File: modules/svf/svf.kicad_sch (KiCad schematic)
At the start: 35 parts, among them U1 VTL5C, U2 VTL5C, U3 MCP6002-xSN, U4 MCP6002-xSN, U5 MCP6002-xSN

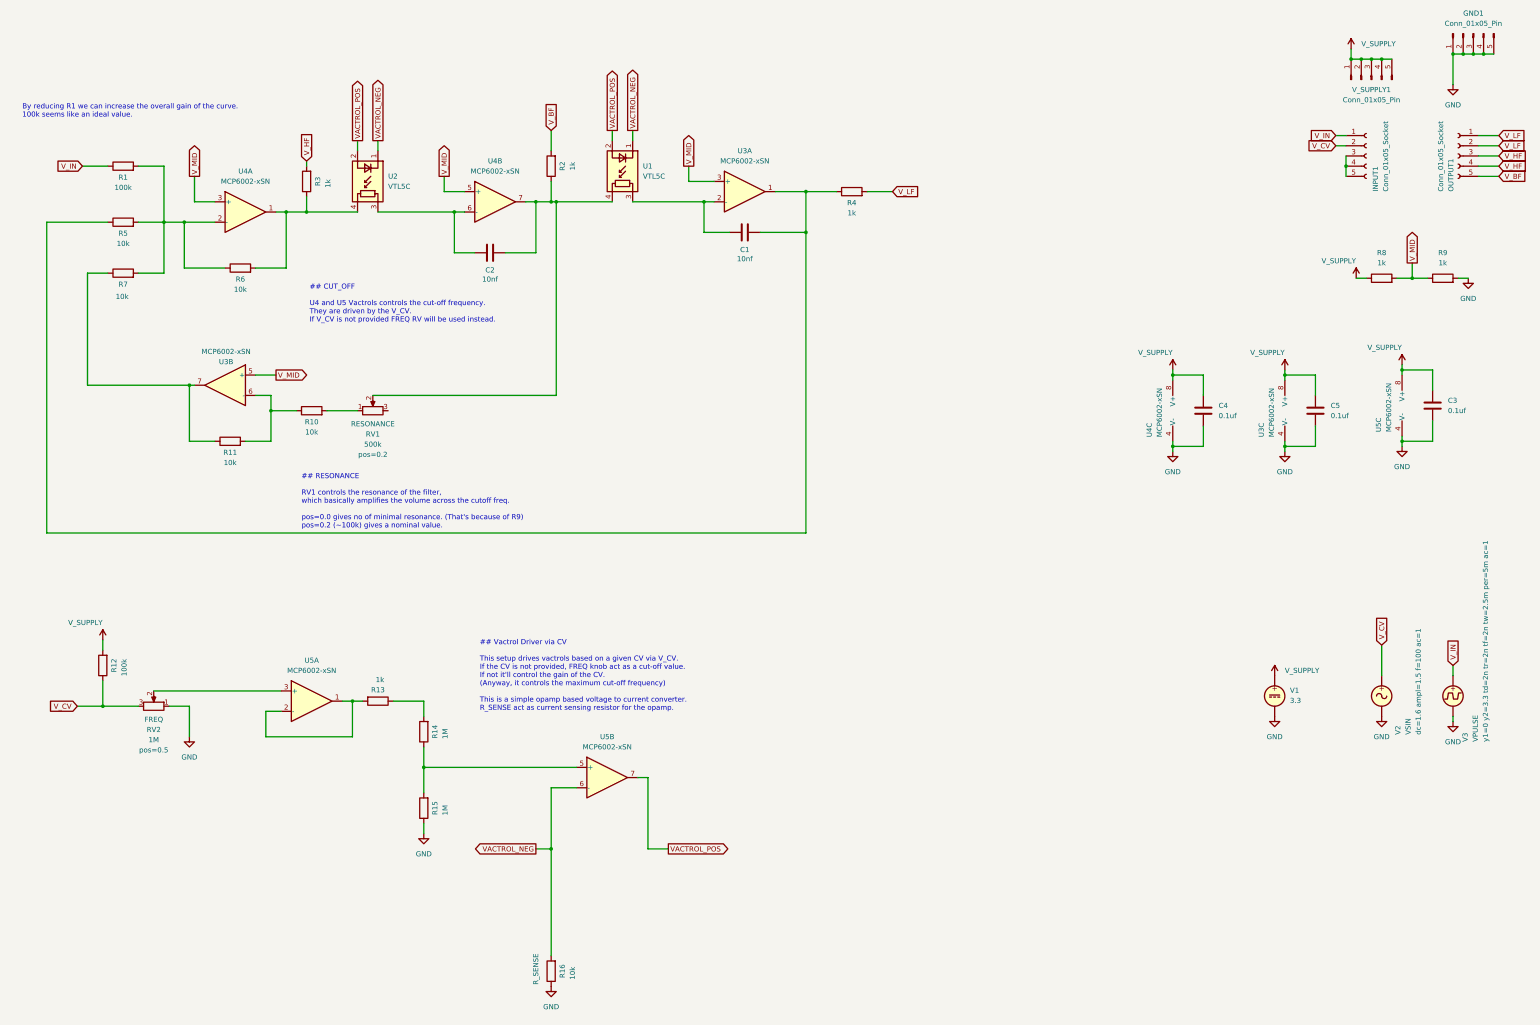
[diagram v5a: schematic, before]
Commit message: Finalized the PCB routing
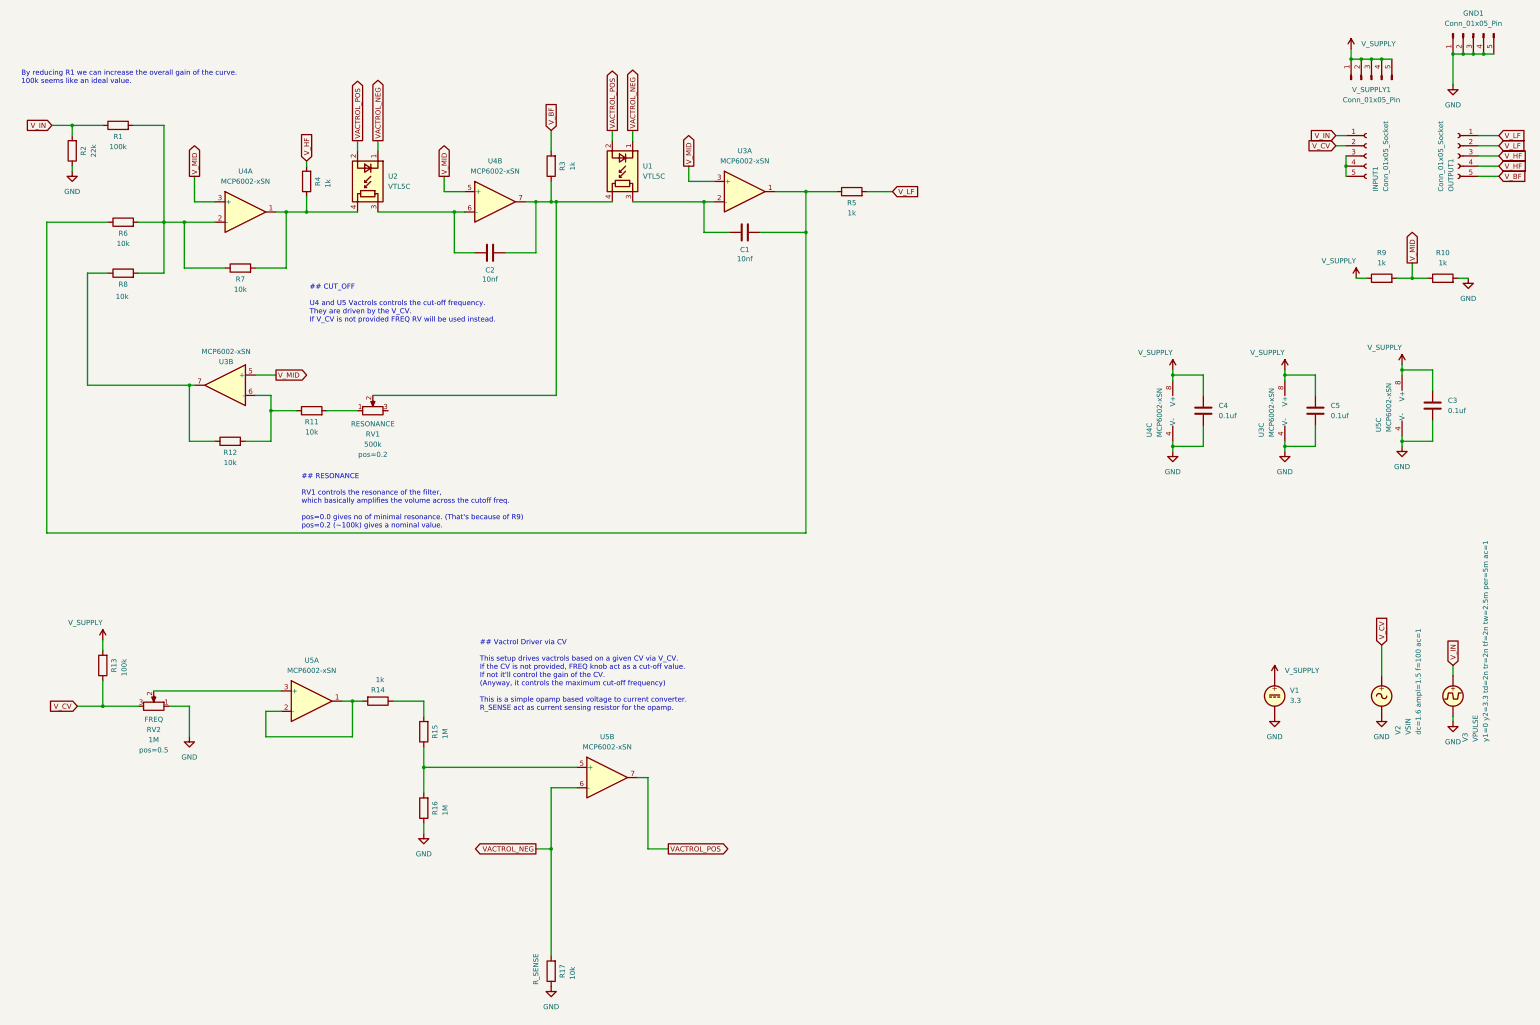
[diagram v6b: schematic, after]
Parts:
- added R2: 22k, Resistor_SMD:R_0402_1005Metric, symbol Device:R
- renumbered R9 to R10, R10 to R11, R11 to R12, R12 to R13, R13 to R14, R14 to R15, R15 to R16, R16 to R17, R2 to R3, R3 to R4, R4 to R5, R5 to R6, R6 to R7, R7 to R8, R8 to R9
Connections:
- net GND: now also R2.1
- net V_IN: now also R2.2
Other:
- moved on the sheet: R1

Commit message: svf: make it louder & add curve control Now the SVF is 8db louder in general. Now the resonance control active troughout the potentiometer Add the curve support for the freq so, we can target low or high based on the usage.
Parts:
- added RV3: 50k, BreadModular_Pots:Potentiometer_RV09, symbol Device:R_Potentiometer
- R1: value 100k -> 51k
- R11, R12: value 10k -> 51k
- R17: value 10k -> 5.1k
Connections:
- net VACTROL_NEG: now also RV3.1; no longer R17.2
- new net: R17.2, RV3.2
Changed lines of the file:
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@@
 	)
 	(junction
-		(at 153.67 226.06)
-		(diameter 0)
-		(color 0 0 0 0)
-	)
-	(junction
 		(at 381 27.94)
 		(diameter 0)
@@
 	)
 	(junction
+		(at 153.67 226.06)
+		(diameter 0)
+		(color 0 0 0 0)
+	)
+	(junction
 		(at 41.91 190.5)
 		(diameter 0)
@@
 	(wire
 		(pts
+			(xy 153.67 246.38) (xy 153.67 252.73)
+		)
+		(stroke
+			(width 0)
+			(type default)
+		)
+	)
+	(wire
+		(pts
 			(xy 27.94 147.32) (xy 217.17 147.32)
 		)
@@
 	(wire
 		(pts
+			(xy 161.29 242.57) (xy 153.67 242.57)
+		)
+		(stroke
+			(width 0)
+			(type default)
+		)
+	)
+	(wire
+		(pts
 			(xy 191.77 64.77) (xy 194.31 64.77)
 		)
@@
 	(wire
 		(pts
+			(xy 153.67 242.57) (xy 153.67 226.06)
+		)
+		(stroke
+			(width 0)
+			(type default)
+		)
+	)
+	(wire
+		(pts
 			(xy 316.23 107.95) (xy 308.61 107.95)
 		)
@@
 	(wire
 		(pts
-			(xy 153.67 226.06) (xy 153.67 252.73)
-		)
-		(stroke
-			(width 0)
-			(type default)
-		)
-	)
-	(wire
-		(pts
 			(xy 54.61 186.69) (xy 86.36 186.69)
 		)
@@
 	(wire
 		(pts
+			(xy 165.1 246.38) (xy 153.67 246.38)
+		)
+		(stroke
+			(width 0)
+			(type default)
+		)
+	)
+	(wire
+		(pts
 			(xy 127 62.23) (xy 127 58.42)
 		)
@@
 	(wire
 		(pts
+			(xy 109.22 113.03) (xy 154.94 113.03)
+		)
+		(stroke
+			(width 0)
+			(type default)
+		)
+	)
+	(wire
+		(pts
 			(xy 383.54 27.94) (xy 386.08 27.94)
 		)
@@
 	(wire
 		(pts
-			(xy 109.22 113.03) (xy 154.94 113.03)
-		)
-		(stroke
-			(width 0)
-			(type default)
-		)
-	)
-	(wire
-		(pts
 			(xy 64.77 58.42) (xy 64.77 64.77)
 		)
@@
 	)
 	(symbol
+		(lib_id "Device:R_Potentiometer")
+		(at 165.1 242.57 90)
+		(mirror x)
+		(unit 1)
+		(exclude_from_sim no)
+		(in_bom yes)
+		(on_board yes)
+		(dnp no)
+		(property "Reference" "RV3"
+			(at 165.1 236.728 90)
+			(effects
+				(font
+					(size 1.27 1.27)
+				)
+			)
+		)
+		(property "Value" "50k"
+			(at 165.1 234.188 90)
+			(effects
+				(font
+					(size 1.27 1.27)
+				)
+			)
+		)
+		(property "Footprint" "BreadModular_Pots:Potentiometer_RV09"
+			(at 165.1 242.57 0)
+			(effects
+				(font
+					(size 1.27 1.27)
+				)
+				(hide yes)
+			)
+		)
+		(property "Datasheet" "~"
+			(at 165.1 242.57 0)
+			(effects
+				(font
+					(size 1.27 1.27)
+				)
+				(hide yes)
+			)
+		)
+		(property "Description" "Potentiometer"
+			(at 165.1 242.57 0)
+			(effects
+				(font
+					(size 1.27 1.27)
+				)
+				(hide yes)
+			)
+		)
+		(property "Sim.Device" "R"
+			(at 165.1 242.57 0)
+			(effects
+				(font
+					(size 1.27 1.27)
+				)
+				(hide yes)
+			)
+		)
+		(property "Sim.Type" "POT"
+			(at 165.1 242.57 0)
+			(effects
+				(font
+					(size 1.27 1.27)
+				)
+				(hide yes)
+			)
+		)
+		(property "Sim.Pins" "1=r0 2=wiper 3=r1"
+			(at 165.1 242.57 0)
+			(effects
+				(font
+					(size 1.27 1.27)
+				)
+				(hide yes)
+			)
+		)
+		(property "Sim.Params" "pos=0.1"
+			(at 165.1 231.648 90)
+			(effects
+				(font
+					(size 1.27 1.27)
+				)
+			)
+		)
+		(property "Comments" "RANGE"
+			(at 165.1 239.268 90)
+			(effects
+				(font
+					(size 1.27 1.27)
+				)
+			)
+		)
+		(pin "3"
+		)
+		(pin "1"
+		)
+		(pin "2"
+		)
+		(instances
+			(project "svf"
+				(path "/b63493d3-5f6d-47e3-845b-87e7090fc1ab"
+					(reference "RV3")
+					(unit 1)
+				)
+			)
+		)
+	)
+	(symbol
 		(lib_id "Simulation_SPICE:VDC")
 		(at 334.01 187.96 0)
@@
 			)
 		)
-		(property "Value" "100k"
+		(property "Value" "51k"
 			(at 45.72 51.054 90)
 			(effects
@@
 			)
 		)
-		(property "Value" "10k"
+		(property "Value" "5.1k"
 			(at 159.004 257.048 90)
 			(effects
@@
 			)
 		)
-		(property "Value" "10k"
+		(property "Value" "51k"
 			(at 73.66 129.794 90)
 			(effects
@@
 			)
 		)
-		(property "Sim.Params" "pos=0.2"
+		(property "Sim.Params" "pos=0.5"
 			(at 109.22 127.762 90)
 			(effects
@@
 			)
 		)
-		(property "Value" "10k"
+		(property "Value" "51k"
 			(at 93.98 122.174 90)
 			(effects
